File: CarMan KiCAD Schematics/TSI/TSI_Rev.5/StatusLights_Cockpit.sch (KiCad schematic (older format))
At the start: 0 parts

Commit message: Update lib, TSAL & CAN/GLV
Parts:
- added C?: 1u, symbol pspice:CAP
- added C?: 4.7u, symbol pspice:CAP
- added D? (x4): Power, symbol Device:D
- added D?: D_Schottky, symbol CarMan_KiCAD_Library:D_Schottky
- added GLV_GND: GLV_GND1, symbol Connector:TestPoint
- added HVPL_LV1: TSAL_LV, symbol Connector:TestPoint
- added Q?: Q_PMOS_DSG, symbol Device:Q_PMOS_DSG
- added Q?: Q_PMOS_GDS, symbol Device:Q_PMOS_GDS
- added R? (x4): 330, symbol Device:R
- added R? (x2): 300, symbol Device:R
- added R? (x2): 10k, symbol Device:R
- added R?: 1M, symbol Device:R
- added R? (x3): R, symbol Device:R
- added U? (x3): TLP293, Package_SO:SOIC-4_4.55x2.6mm_P1.27mm, symbol TSI_Rev.5-rescue:TLP293-CarMan_KiCAD_Library
- added U?: RDE03110S12, symbol CarMan_KiCAD_Library:RDE03110S12
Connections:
- net labels added: +24V, +3.3V, +5V, BP, BP_RTN, Cooling_CTRL, D_LED_CTRL, Drive_BTN, Drive_BTN_RTN, Drive_LED, HV+, HV-, Heartbeat, IMD_Fault_LED, IMD_Status, LV_RTN, PC_ready, RTDS, RTDS_CTRL, RTDS_RTN, SPARE_LED, SPARE_LED_CTRL, Spare_Blue, Spare_Red, TSAL_1, TSAL_Cock
- wire segments 0 -> 102
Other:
- note added: "*NOTE* LEDs will be repurposed"
- note added: "0.2A Id *CHECK THIS FET, specifications\n are likely not correct.\n Placeholder transistor*"
- note added: "0.3A Id *CHECK THIS FET, specifications\n are likely not correct. Placeholder transistor*"
- note added: "Current Ratio 50%"
- note added: "HIGH VOLTAGE\n"
- note added: "STA20502 RTDS BUZZER (.6A MAX)\n"

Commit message: TSI Fixes - Hi Neal
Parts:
- U? (x3): symbol TSI_Rev.5-rescue:TLP293-CarMan_KiCAD_Library -> TSI_Rev.5-rescue:TLP293-CarMan_KiCAD_Library-TSI_Rev.5-rescue
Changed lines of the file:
@@
 EESchema Schematic File Version 4
-EELAYER 30 0
+LIBS:TSI_Rev.5-cache
+EELAYER 29 0
 EELAYER END
 $Descr A4 11693 8268
 encoding utf-8
-Sheet 6 6
+Sheet 2 6
 Title ""
 Date ""
@@
 LV_RTN
 $Comp
-L TSI_Rev.5-rescue:TLP293-CarMan_KiCAD_Library U?
+L TSI_Rev.5-rescue:TLP293-CarMan_KiCAD_Library-TSI_Rev.5-rescue U?
 U 1 1 5F9A966C
 P 4550 2350
@@
 $EndComp
 $Comp
-L TSI_Rev.5-rescue:TLP293-CarMan_KiCAD_Library U?
+L TSI_Rev.5-rescue:TLP293-CarMan_KiCAD_Library-TSI_Rev.5-rescue U?
 U 1 1 5F9AA400
 P 4550 3150
@@
 	4250 1300 3800 1300
 $Comp
-L TSI_Rev.5-rescue:TLP293-CarMan_KiCAD_Library U?
+L TSI_Rev.5-rescue:TLP293-CarMan_KiCAD_Library-TSI_Rev.5-rescue U?
 U 1 1 5F9B7294
 P 4550 1400

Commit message: Goopdate
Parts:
- removed D? (x3): Power, symbol Device:D
- removed R? (x3): 330, symbol Device:R
- GLV_RTN: renamed from GLV_GND; value GLV_GND1 -> GLV_RTN
- R25: renamed from R?; value R -> 300
- gave numbers to parts that had none: 7
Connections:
- net labels added: 24V, 3.3V, 5V, AMS_FAULT_LED, FAULT_LED_RTN, GLV_RTN, IMD_FAULT_LED, TSAL, TSAL_Cockpit, TSAL_RTN
- net labels removed: +24V, +5V, Cooling_CTRL, Heartbeat, PC_ready, Spare_Blue, Spare_Red, TSAL_1, TSAL_Cock
- wire segments 102 -> 92
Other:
- note added: "needs to be addressed\n"
- note removed: "*NOTE* LEDs will be repurposed"
- moved on the sheet: D?, R?

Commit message: Fixed More TSI connections/renamed things
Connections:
- net labels removed: +3.3V, LV_RTN
- wire segments 92 -> 94
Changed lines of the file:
@@
 EESchema Schematic File Version 4
-EELAYER 30 0
+LIBS:TSI_Rev.5-cache
+EELAYER 29 0
 EELAYER END
 $Descr A4 11693 8268
@@
 	7600 5350 7350 5350
 Text Label 7350 5000 2    50   ~ 0
-+3.3V
+3.3V
 Text Label 7350 5350 2    50   ~ 0
 Drive_BTN
@@
 Drive_BTN_RTN
 Text Label 8700 5000 2    50   ~ 0
-LV_RTN
+GLV_RTN
 Wire Notes Line
 	8050 5000 8100 5000
@@
 Text Label 1600 3250 0    50   ~ 0
 AMS_FAULT_LED
+Text HLabel 1200 2300 0    50   Input ~ 0
+Drive_BTN_RTN
+Wire Wire Line
+	1200 2300 1350 2300
+Text Label 1350 2300 0    50   ~ 0
+Drive_BTN_RTN
+Text HLabel 1200 2200 0    50   Input ~ 0
+Drive_BTN
+Wire Wire Line
+	1200 2200 1350 2200
+Text Label 1350 2200 0    50   ~ 0
+Drive_BTN
 $EndSCHEMATC

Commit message: Soupdate
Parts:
- Q1: renamed from Q?; value Q_PMOS_GDS -> ZVP0545G
- Q3: renamed from Q?; value Q_PMOS_DSG -> ZVP1320F
- R17: renamed from R?; value 10k -> 10K
- gave numbers to parts that had none: 6
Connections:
- net labels added: Brake_Pressed, Brake_Pressed_RTN
- net labels removed: BP, BP_RTN
- wire segments 94 -> 86
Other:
- note added: "IMD TRANSISTOR"
- note added: "SIGNALS\n"
- moved on the sheet: C14, C17, D11, Q1, R110, R12, R15, R17, R25, R74, R?, U1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

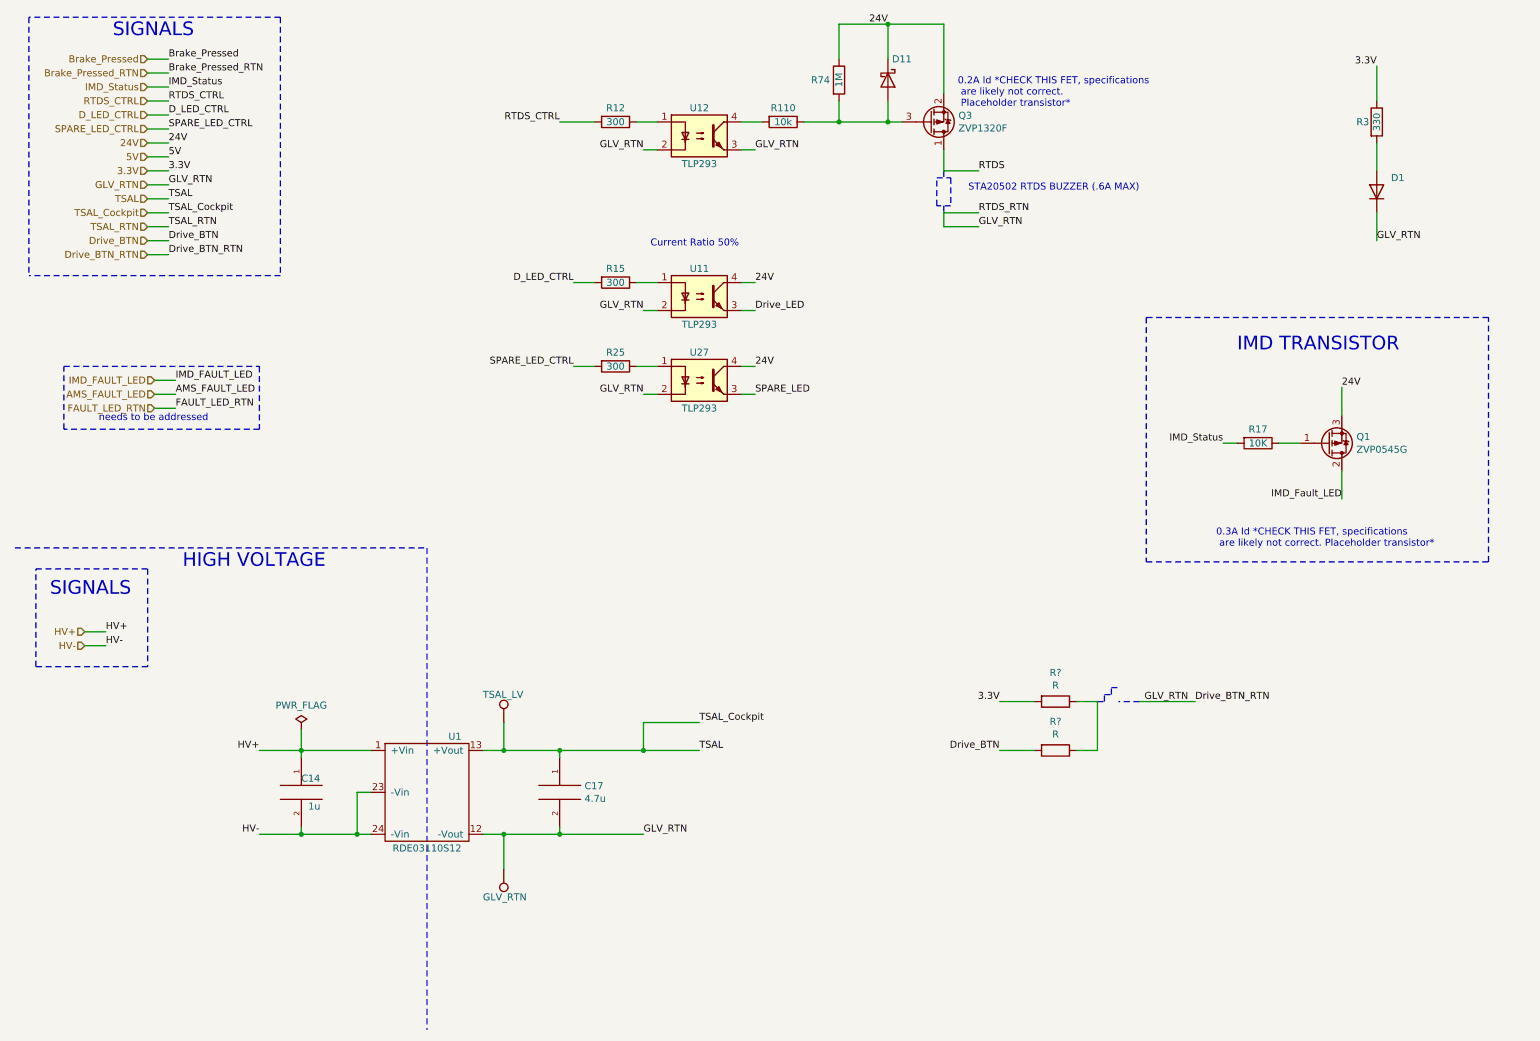
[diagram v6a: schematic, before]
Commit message: TSI - Added 24V- 5v isolated converter, Scada relay, and fixed connections
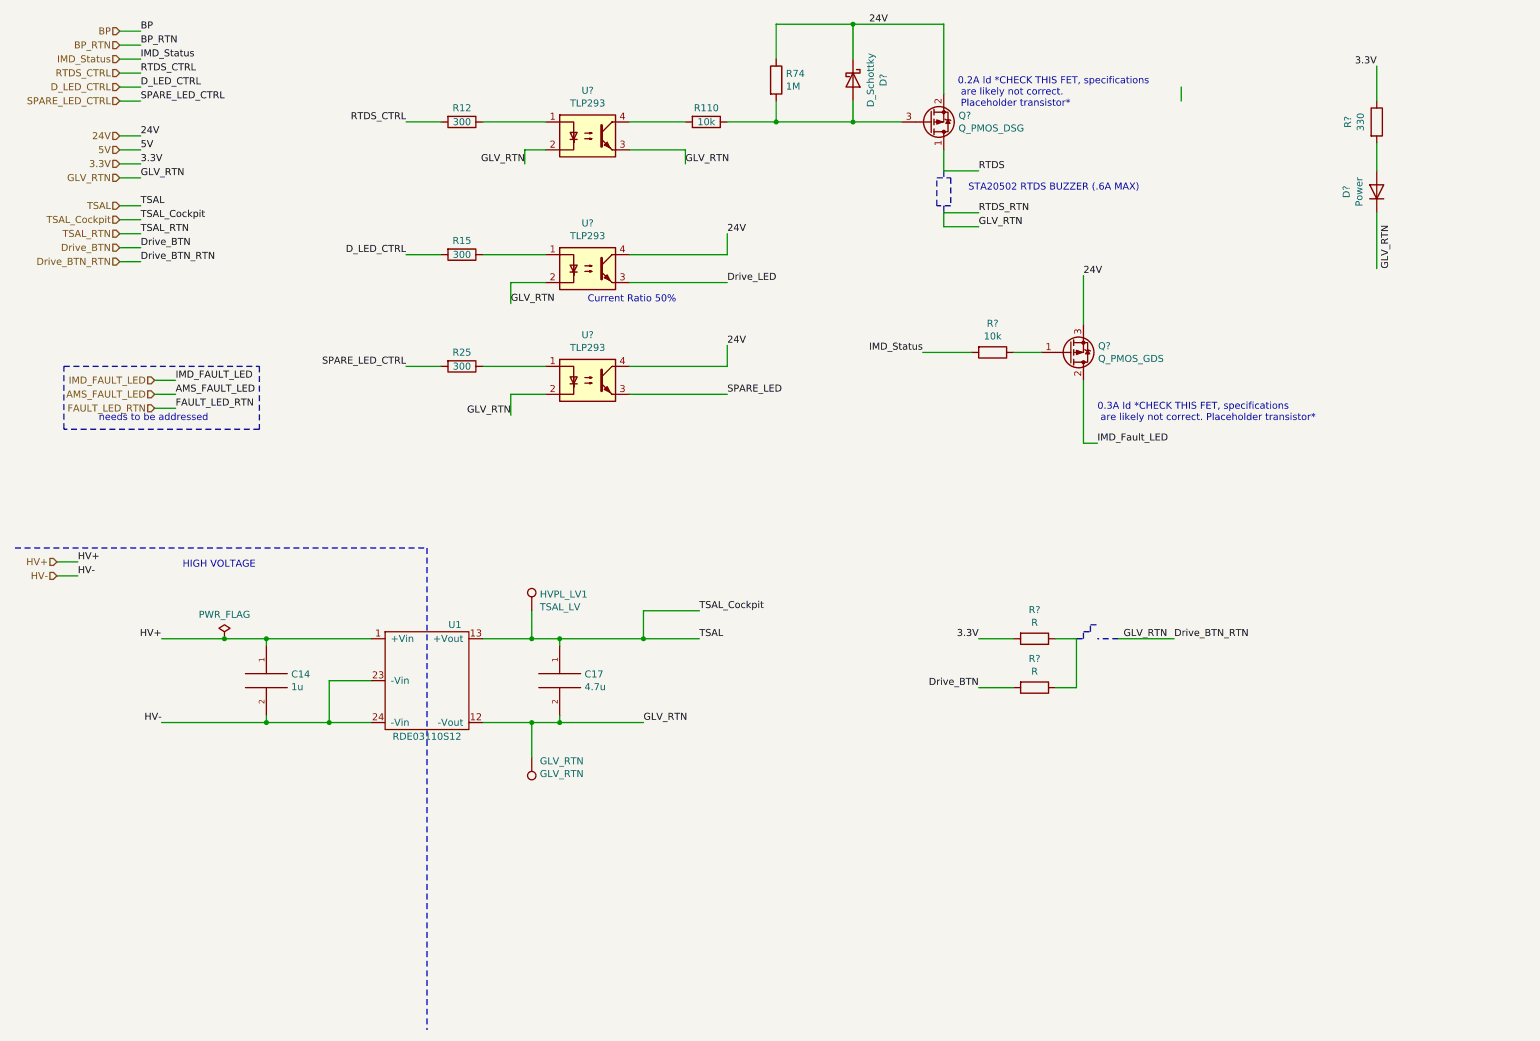
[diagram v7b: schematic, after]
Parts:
- Q?: renamed from Q3; value ZVP1320F -> Q_PMOS_DSG
- Q?: renamed from Q1; value ZVP0545G -> Q_PMOS_GDS
- R?: renamed from R17; value 10K -> 10k
- renumbered D1 to D?, D11 to D?, R3 to R?, U11 to U?, U27 to U?, U12 to U?
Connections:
- net labels added: BP, BP_RTN
- net labels removed: Brake_Pressed, Brake_Pressed_RTN
- wire segments 86 -> 94
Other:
- note removed: "IMD TRANSISTOR"
- note removed: "SIGNALS\n"
- moved on the sheet: C14, C17, D?, Q?, R110, R12, R15, R25, R74, R?, U1, U?
